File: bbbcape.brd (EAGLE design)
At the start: 54.6 x 71.8 mm, 25 parts

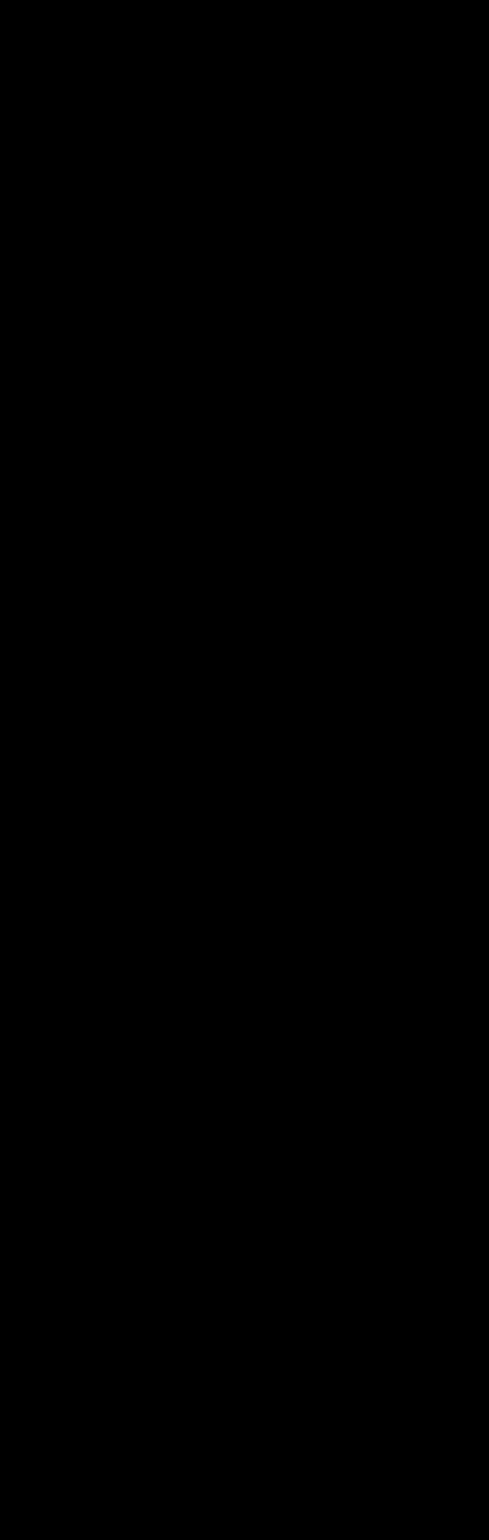
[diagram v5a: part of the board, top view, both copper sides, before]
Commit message: Added and connected firing circuit.
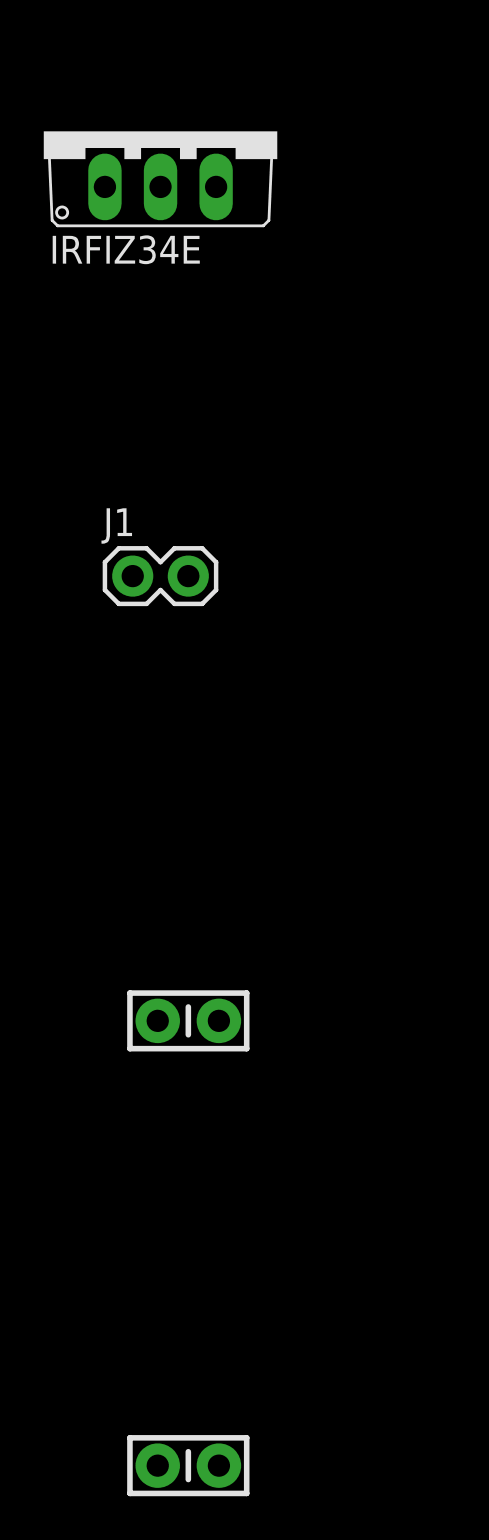
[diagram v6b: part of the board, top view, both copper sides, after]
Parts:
- added C2, C3: (no value), SparkFun-Capacitors:CAP-PTH-SMALL-KIT
- added IRFIZ34E: (no value), adafruit:TO220V
- added J1: (no value), SparkFun-Connectors:1X02
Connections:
- removed net 6V5: 6V5O.1, 6V5O.2
- removed net N$1: 5VI.1, 5VI.2, 6V5I.1, 6V5I.2, BATT.2, C1.1
- new net FEU: BBB.69, IRFIZ34E.1
- new net N$3: IRFIZ34E.2, J1.1
- new net VBAT: 5VI.1, 5VI.2, 6V5I.1, 6V5I.2, BATT.2, C1.1, C2.2
- net GND: now also C2.1, C3.2, IRFIZ34E.3
- net VCC: now also 6V5O.1, 6V5O.2, C3.1, J1.2
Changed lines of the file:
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@@
 <element name="R8" library="SparkFun-Passives" package="AXIAL-0.3" value="670" x="-78.74" y="-257.81"/>
 <element name="R9" library="SparkFun-Passives" package="AXIAL-0.3" value="1k" x="-78.74" y="-276.86"/>
+<element name="IRFIZ34E" library="adafruit" package="TO220V" value="" x="-81.28" y="-292.1"/>
+<element name="J1" library="SparkFun-Connectors" package="1X02" value="" x="-82.55" y="-312.42"/>
+<element name="C2" library="SparkFun-Capacitors" package="CAP-PTH-SMALL-KIT" value="" x="-80.01" y="-332.74">
+<attribute name="PROD_ID" value="CAP-08370" x="-80.01" y="-332.74" size="1.778" layer="27" display="off"/>
+</element>
+<element name="C3" library="SparkFun-Capacitors" package="CAP-PTH-SMALL-KIT" value="" x="-80.01" y="-353.06">
+<attribute name="PROD_ID" value="CAP-08370" x="-80.01" y="-353.06" size="1.778" layer="27" display="off"/>
+</element>
 </elements>
 <signals>
@@
 <contactref element="R9" pad="P$1"/>
 <contactref element="SHLD1" pad="8"/>
+<contactref element="C2" pad="1"/>
+<contactref element="IRFIZ34E" pad="3"/>
+<contactref element="C3" pad="2"/>
 <wire x1="-82.55" y1="-200.66" x2="-82.55" y2="-162.56" width="0" layer="19" extent="1-1"/>
 <wire x1="-82.55" y1="-238.76" x2="-82.55" y2="-200.66" width="0" layer="19" extent="1-1"/>
 <wire x1="-82.55" y1="-276.86" x2="-82.55" y2="-238.76" width="0" layer="19" extent="1-1"/>
+<wire x1="-78.74" y1="-294.64" x2="-82.55" y2="-276.86" width="0" layer="19" extent="1-1"/>
+<wire x1="-81.407" y1="-332.74" x2="-78.74" y2="-294.64" width="0" layer="19" extent="1-1"/>
+<wire x1="-78.613" y1="-353.06" x2="-81.407" y2="-332.74" width="0" layer="19" extent="1-1"/>
 <wire x1="-82.55" y1="-67.31" x2="-82.55" y2="-162.56" width="0" layer="19" extent="1-1"/>
 <wire x1="-82.55" y1="-48.26" x2="-82.55" y2="-67.31" width="0" layer="19" extent="1-1"/>
@@
 <wire x1="-77.47" y1="90.17" x2="-74.93" y2="90.17" width="0" layer="19" extent="1-1"/>
 </signal>
-<signal name="N$1">
+<signal name="VBAT">
 <contactref element="BATT" pad="2"/>
 <contactref element="5VI" pad="1"/>
@@
 <contactref element="6V5I" pad="1"/>
 <contactref element="C1" pad="1"/>
+<contactref element="C2" pad="2"/>
+<wire x1="-72.39" y1="3.81" x2="-78.613" y2="-332.74" width="0" layer="19" extent="1-1"/>
 <wire x1="-80.01" y1="90.17" x2="-72.39" y2="3.81" width="0" layer="19" extent="1-1"/>
 <wire x1="-82.55" y1="90.17" x2="-80.01" y2="90.17" width="0" layer="19" extent="1-1"/>
@@
 <wire x1="-49.53" y1="90.17" x2="-52.07" y2="95.25" width="0" layer="19" extent="1-1"/>
 <wire x1="-46.99" y1="90.17" x2="-49.53" y2="90.17" width="0" layer="19" extent="1-1"/>
-</signal>
-<signal name="6V5">
-<contactref element="6V5O" pad="1"/>
-<contactref element="6V5O" pad="2"/>
-<wire x1="-27.94" y1="95.25" x2="-25.4" y2="95.25" width="0" layer="19" extent="1-1"/>
 </signal>
 <signal name="5V">
@@
 <signal name="VCC">
 <contactref element="CAM" pad="2"/>
+<contactref element="6V5O" pad="1"/>
+<contactref element="6V5O" pad="2"/>
+<contactref element="C3" pad="1"/>
+<contactref element="J1" pad="2"/>
+<wire x1="-80.01" y1="-312.42" x2="-81.407" y2="-353.06" width="0" layer="19" extent="1-1"/>
+<wire x1="-80.01" y1="-48.26" x2="-80.01" y2="-312.42" width="0" layer="19" extent="1-1"/>
+<wire x1="-27.94" y1="95.25" x2="-80.01" y2="-48.26" width="0" layer="19" extent="1-1"/>
+<wire x1="-25.4" y1="95.25" x2="-27.94" y2="95.25" width="0" layer="19" extent="1-1"/>
 </signal>
 <signal name="UART1_TX">
@@
 <wire x1="-66.04" y1="90.17" x2="-63.5" y2="90.17" width="0" layer="19" extent="1-1"/>
 </signal>
+<signal name="N$3">
+<contactref element="IRFIZ34E" pad="2"/>
+<contactref element="J1" pad="1"/>
+<wire x1="-81.28" y1="-294.64" x2="-82.55" y2="-312.42" width="0" layer="19" extent="1-1"/>
+</signal>
+<signal name="FEU">
+<contactref element="BBB" pad="69"/>
+<contactref element="IRFIZ34E" pad="1"/>
+<wire x1="52.07" y1="29.21" x2="-83.82" y2="-294.64" width="0" layer="19" extent="1-1"/>
+</signal>
 </signals>

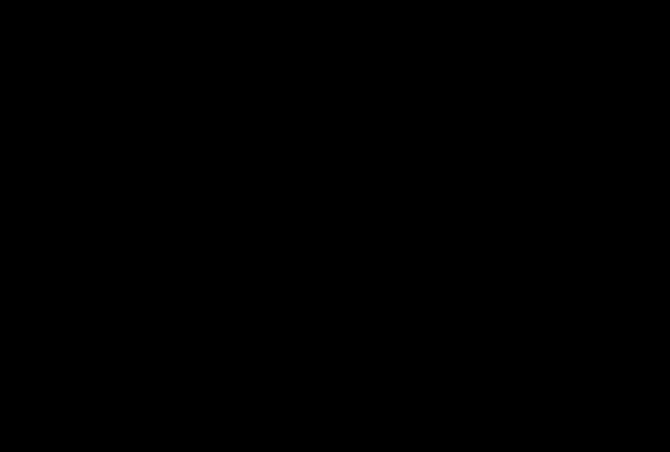
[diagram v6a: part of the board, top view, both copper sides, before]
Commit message: Added reset button (on BAR_GA, P8_10).
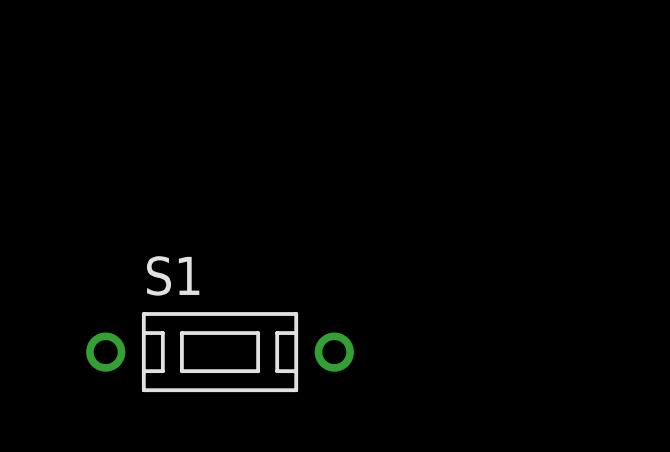
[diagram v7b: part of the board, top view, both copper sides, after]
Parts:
- added S1: TACTILE-SPST-6MM-SLIM, michel:6MM-SLIM
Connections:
- net BAR_GA: now also S1.P$2
- net BCOM: now also S1.P$1
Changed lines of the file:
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@@
 <attribute name="PROD_ID" value="CAP-08370" x="-80.01" y="-353.06" size="1.778" layer="27" display="off"/>
 </element>
+<element name="S1" library="michel" package="6MM-SLIM" value="TACTILE-SPST-6MM-SLIM" x="-81.28" y="-370.84"/>
 </elements>
 <signals>
@@
 <contactref element="R1" pad="P$1"/>
 <contactref element="BBB" pad="12"/>
+<contactref element="S1" pad="P$1"/>
+<wire x1="1.27" y1="13.97" x2="-85.09" y2="-370.84" width="0" layer="19" extent="1-1"/>
+<wire x1="-41.91" y1="95.25" x2="1.27" y2="13.97" width="0" layer="19" extent="1-1"/>
 <wire x1="-66.04" y1="95.25" x2="-41.91" y2="95.25" width="0" layer="19" extent="1-1"/>
-<wire x1="1.27" y1="13.97" x2="-41.91" y2="95.25" width="0" layer="19" extent="1-1"/>
 </signal>
 <signal name="BAV_DR">
@@
 <contactref element="BPR" pad="5"/>
 <contactref element="BBB" pad="10"/>
-<wire x1="1.27" y1="11.43" x2="-31.75" y2="95.25" width="0" layer="19" extent="1-1"/>
+<contactref element="S1" pad="P$2"/>
+<wire x1="1.27" y1="11.43" x2="-77.47" y2="-370.84" width="0" layer="19" extent="1-1"/>
+<wire x1="-31.75" y1="95.25" x2="1.27" y2="11.43" width="0" layer="19" extent="1-1"/>
 </signal>
 <signal name="3.3V">

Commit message: Added new DC-DC converter symbol (instead of headers).
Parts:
- removed 5VI, 5VO, 6V5I, 6V5O: (no value), SparkFun-Connectors:1X06
- added U5V, U6V5: SEEED-MP1584, michel:SEEED-MP1584
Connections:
- net GND: now also U5V.IN0+, U5V.IN1+, U5V.OUT0+, U5V.OUT1+, U6V5.IN0-, U6V5.IN1-, U6V5.OUT0-, U6V5.OUT1-; no longer 5VI.3, 5VI.4, 5VI.5, 5VI.6, 5VO.3, 5VO.4, 5VO.5, 5VO.6, 6V5I.3, 6V5I.4, 6V5I.5, 6V5I.6, 6V5O.3, 6V5O.4, 6V5O.5, 6V5O.6
- net VBAT: now also U5V.IN0-, U5V.IN1-, U6V5.IN0+, U6V5.IN1+; no longer 5VI.1, 5VI.2, 6V5I.1, 6V5I.2
- net VCC: now also U6V5.OUT0+, U6V5.OUT1+; no longer 6V5O.1, 6V5O.2
- net VDD: now also U5V.OUT0-, U5V.OUT1-; no longer 5VO.1, 5VO.2
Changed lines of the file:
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@@
 </autorouter>
 <elements>
-<element name="5VI" library="SparkFun-Connectors" package="1X06" value="" x="-49.53" y="90.17">
-<attribute name="PROD_ID" value="CONN-08437" x="-49.53" y="90.17" size="1.778" layer="27" display="off"/>
-</element>
-<element name="5VO" library="SparkFun-Connectors" package="1X06" value="" x="-66.04" y="90.17">
-<attribute name="PROD_ID" value="CONN-08437" x="-66.04" y="90.17" size="1.778" layer="27" display="off"/>
-</element>
-<element name="6V5I" library="SparkFun-Connectors" package="1X06" value="" x="-82.55" y="90.17">
-<attribute name="PROD_ID" value="CONN-08437" x="-82.55" y="90.17" size="1.778" layer="27" display="off"/>
-</element>
-<element name="6V5O" library="SparkFun-Connectors" package="1X06" value="" x="-27.94" y="95.25">
-<attribute name="PROD_ID" value="CONN-08437" x="-27.94" y="95.25" size="1.778" layer="27" display="off"/>
-</element>
 <element name="BATT" library="SparkFun-Connectors" package="1X02" value="" x="-54.61" y="95.25"/>
 <element name="BBB" library="adafruit" package="BEAGLEBONE_SHIELD" value="BEAGLEBONE_OUTLINE" x="-0.635" y="-17.78"/>
@@
 </element>
 <element name="S1" library="michel" package="6MM-SLIM" value="TACTILE-SPST-6MM-SLIM" x="-81.28" y="-370.84"/>
+<element name="U6V5" library="michel" package="SEEED-MP1584" value="SEEED-MP1584" x="-74.93" y="-391.16"/>
+<element name="U5V" library="michel" package="SEEED-MP1584" value="SEEED-MP1584" x="-74.93" y="-417.83"/>
 </elements>
 <signals>
@@
 <contactref element="BATT" pad="1"/>
 <contactref element="C1" pad="2"/>
-<contactref element="6V5I" pad="3"/>
-<contactref element="6V5I" pad="4"/>
-<contactref element="6V5I" pad="5"/>
-<contactref element="6V5I" pad="6"/>
-<contactref element="6V5O" pad="3"/>
-<contactref element="6V5O" pad="6"/>
-<contactref element="6V5O" pad="5"/>
-<contactref element="6V5O" pad="4"/>
-<contactref element="5VI" pad="3"/>
-<contactref element="5VI" pad="4"/>
-<contactref element="5VI" pad="5"/>
-<contactref element="5VI" pad="6"/>
-<contactref element="5VO" pad="3"/>
-<contactref element="5VO" pad="4"/>
-<contactref element="5VO" pad="5"/>
-<contactref element="5VO" pad="6"/>
 <contactref element="CAM" pad="1"/>
 <contactref element="R3" pad="P$1"/>
@@
 <contactref element="IRFIZ34E" pad="3"/>
 <contactref element="C3" pad="2"/>
-<wire x1="-82.55" y1="-200.66" x2="-82.55" y2="-162.56" width="0" layer="19" extent="1-1"/>
-<wire x1="-82.55" y1="-238.76" x2="-82.55" y2="-200.66" width="0" layer="19" extent="1-1"/>
-<wire x1="-82.55" y1="-276.86" x2="-82.55" y2="-238.76" width="0" layer="19" extent="1-1"/>
-<wire x1="-78.74" y1="-294.64" x2="-82.55" y2="-276.86" width="0" layer="19" extent="1-1"/>
-<wire x1="-81.407" y1="-332.74" x2="-78.74" y2="-294.64" width="0" layer="19" extent="1-1"/>
-<wire x1="-78.613" y1="-353.06" x2="-81.407" y2="-332.74" width="0" layer="19" extent="1-1"/>
+<contactref element="U6V5" pad="OUT0-"/>
+<contactref element="U6V5" pad="OUT1-"/>
+<contactref element="U6V5" pad="IN0-"/>
+<contactref element="U6V5" pad="IN1-"/>
+<contactref element="U5V" pad="OUT1+"/>
+<contactref element="U5V" pad="OUT0+"/>
+<contactref element="U5V" pad="IN1+"/>
+<contactref element="U5V" pad="IN0+"/>
+<wire x1="-84.18" y1="-424.455" x2="-84.18" y2="-421.83" width="0" layer="19" extent="1-1"/>
+<wire x1="-65.68" y1="-424.455" x2="-84.18" y2="-424.455" width="0" layer="19" extent="1-1"/>
+<wire x1="-65.68" y1="-421.83" x2="-65.68" y2="-424.455" width="0" layer="19" extent="1-1"/>
+<wire x1="-84.18" y1="-387.16" x2="-84.18" y2="-421.83" width="0" layer="19" extent="1-1"/>
+<wire x1="-84.18" y1="-384.535" x2="-84.18" y2="-387.16" width="0" layer="19" extent="1-1"/>
+<wire x1="-65.68" y1="-387.16" x2="-84.18" y2="-387.16" width="0" layer="19" extent="1-1"/>
+<wire x1="-65.68" y1="-384.535" x2="-65.68" y2="-387.16" width="0" layer="19" extent="1-1"/>
+<wire x1="-78.613" y1="-353.06" x2="-84.18" y2="-384.535" width="0" layer="19" extent="1-1"/>
+<wire x1="-81.407" y1="-332.74" x2="-78.613" y2="-353.06" width="0" layer="19" extent="1-1"/>
+<wire x1="-78.74" y1="-294.64" x2="-81.407" y2="-332.74" width="0" layer="19" extent="1-1"/>
+<wire x1="-82.55" y1="-276.86" x2="-78.74" y2="-294.64" width="0" layer="19" extent="1-1"/>
+<wire x1="-82.55" y1="-238.76" x2="-82.55" y2="-276.86" width="0" layer="19" extent="1-1"/>
+<wire x1="-82.55" y1="-200.66" x2="-82.55" y2="-238.76" width="0" layer="19" extent="1-1"/>
+<wire x1="-82.55" y1="-162.56" x2="-82.55" y2="-200.66" width="0" layer="19" extent="1-1"/>
 <wire x1="-82.55" y1="-67.31" x2="-82.55" y2="-162.56" width="0" layer="19" extent="1-1"/>
 <wire x1="-82.55" y1="-48.26" x2="-82.55" y2="-67.31" width="0" layer="19" extent="1-1"/>
@@
 <wire x1="49.53" y1="54.61" x2="52.07" y2="54.61" width="0" layer="19" extent="1-1"/>
 <wire x1="-15.24" y1="90.17" x2="49.53" y2="57.15" width="0" layer="19" extent="1-1"/>
-<wire x1="-15.24" y1="95.25" x2="-15.24" y2="90.17" width="0" layer="19" extent="1-1"/>
-<wire x1="-17.78" y1="95.25" x2="-15.24" y2="95.25" width="0" layer="19" extent="1-1"/>
-<wire x1="-20.32" y1="95.25" x2="-17.78" y2="95.25" width="0" layer="19" extent="1-1"/>
-<wire x1="-22.86" y1="95.25" x2="-20.32" y2="95.25" width="0" layer="19" extent="1-1"/>
-<wire x1="-36.83" y1="90.17" x2="-22.86" y2="95.25" width="0" layer="19" extent="1-1"/>
-<wire x1="-39.37" y1="90.17" x2="-36.83" y2="90.17" width="0" layer="19" extent="1-1"/>
-<wire x1="-41.91" y1="90.17" x2="-39.37" y2="90.17" width="0" layer="19" extent="1-1"/>
-<wire x1="-44.45" y1="90.17" x2="-41.91" y2="90.17" width="0" layer="19" extent="1-1"/>
-<wire x1="-48.26" y1="95.25" x2="-44.45" y2="90.17" width="0" layer="19" extent="1-1"/>
+<wire x1="-48.26" y1="95.25" x2="-15.24" y2="90.17" width="0" layer="19" extent="1-1"/>
 <wire x1="-54.61" y1="95.25" x2="-48.26" y2="95.25" width="0" layer="19" extent="1-1"/>
-<wire x1="-53.34" y1="90.17" x2="-54.61" y2="95.25" width="0" layer="19" extent="1-1"/>
-<wire x1="-55.88" y1="90.17" x2="-53.34" y2="90.17" width="0" layer="19" extent="1-1"/>
-<wire x1="-58.42" y1="90.17" x2="-55.88" y2="90.17" width="0" layer="19" extent="1-1"/>
-<wire x1="-60.96" y1="90.17" x2="-58.42" y2="90.17" width="0" layer="19" extent="1-1"/>
-<wire x1="-69.85" y1="90.17" x2="-60.96" y2="90.17" width="0" layer="19" extent="1-1"/>
-<wire x1="-72.39" y1="90.17" x2="-69.85" y2="90.17" width="0" layer="19" extent="1-1"/>
-<wire x1="-74.93" y1="90.17" x2="-72.39" y2="90.17" width="0" layer="19" extent="1-1"/>
-<wire x1="-77.47" y1="90.17" x2="-74.93" y2="90.17" width="0" layer="19" extent="1-1"/>
 </signal>
 <signal name="VBAT">
 <contactref element="BATT" pad="2"/>
-<contactref element="5VI" pad="1"/>
-<contactref element="5VI" pad="2"/>
-<contactref element="6V5I" pad="2"/>
-<contactref element="6V5I" pad="1"/>
+<contactref element="C2" pad="2"/>
+<contactref element="U5V" pad="IN1-"/>
+<contactref element="U5V" pad="IN0-"/>
+<contactref element="U6V5" pad="IN0+"/>
+<contactref element="U6V5" pad="IN1+"/>
 <contactref element="C1" pad="1"/>
-<contactref element="C2" pad="2"/>
+<wire x1="-84.18" y1="-411.205" x2="-84.18" y2="-413.83" width="0" layer="19" extent="1-1"/>
+<wire x1="-84.18" y1="-397.785" x2="-84.18" y2="-411.205" width="0" layer="19" extent="1-1"/>
+<wire x1="-84.18" y1="-395.16" x2="-84.18" y2="-397.785" width="0" layer="19" extent="1-1"/>
+<wire x1="-78.613" y1="-332.74" x2="-84.18" y2="-395.16" width="0" layer="19" extent="1-1"/>
 <wire x1="-72.39" y1="3.81" x2="-78.613" y2="-332.74" width="0" layer="19" extent="1-1"/>
-<wire x1="-80.01" y1="90.17" x2="-72.39" y2="3.81" width="0" layer="19" extent="1-1"/>
-<wire x1="-82.55" y1="90.17" x2="-80.01" y2="90.17" width="0" layer="19" extent="1-1"/>
-<wire x1="-52.07" y1="95.25" x2="-80.01" y2="90.17" width="0" layer="19" extent="1-1"/>
-<wire x1="-49.53" y1="90.17" x2="-52.07" y2="95.25" width="0" layer="19" extent="1-1"/>
-<wire x1="-46.99" y1="90.17" x2="-49.53" y2="90.17" width="0" layer="19" extent="1-1"/>
+<wire x1="-52.07" y1="95.25" x2="-72.39" y2="3.81" width="0" layer="19" extent="1-1"/>
 </signal>
 <signal name="5V">
@@
 <signal name="VCC">
 <contactref element="CAM" pad="2"/>
-<contactref element="6V5O" pad="1"/>
-<contactref element="6V5O" pad="2"/>
 <contactref element="C3" pad="1"/>
 <contactref element="J1" pad="2"/>
+<contactref element="U6V5" pad="OUT0+"/>
+<contactref element="U6V5" pad="OUT1+"/>
+<wire x1="-65.68" y1="-395.16" x2="-65.68" y2="-397.785" width="0" layer="19" extent="1-1"/>
+<wire x1="-81.407" y1="-353.06" x2="-65.68" y2="-395.16" width="0" layer="19" extent="1-1"/>
 <wire x1="-80.01" y1="-312.42" x2="-81.407" y2="-353.06" width="0" layer="19" extent="1-1"/>
 <wire x1="-80.01" y1="-48.26" x2="-80.01" y2="-312.42" width="0" layer="19" extent="1-1"/>
-<wire x1="-27.94" y1="95.25" x2="-80.01" y2="-48.26" width="0" layer="19" extent="1-1"/>
-<wire x1="-25.4" y1="95.25" x2="-27.94" y2="95.25" width="0" layer="19" extent="1-1"/>
 </signal>
 <signal name="UART1_TX">
@@
 <signal name="VDD">
 <contactref element="BBB" pad="51"/>
-<contactref element="5VO" pad="1"/>
-<contactref element="5VO" pad="2"/>
 <contactref element="BBB" pad="52"/>
-<wire x1="49.53" y1="6.35" x2="52.07" y2="6.35" width="0" layer="19" extent="1-1"/>
-<wire x1="-63.5" y1="90.17" x2="49.53" y2="6.35" width="0" layer="19" extent="1-1"/>
-<wire x1="-66.04" y1="90.17" x2="-63.5" y2="90.17" width="0" layer="19" extent="1-1"/>
+<contactref element="U5V" pad="OUT1-"/>
+<contactref element="U5V" pad="OUT0-"/>
+<wire x1="-65.68" y1="-411.205" x2="-65.68" y2="-413.83" width="0" layer="19" extent="1-1"/>
+<wire x1="49.53" y1="6.35" x2="-65.68" y2="-411.205" width="0" layer="19" extent="1-1"/>
+<wire x1="52.07" y1="6.35" x2="49.53" y2="6.35" width="0" layer="19" extent="1-1"/>
 </signal>
 <signal name="N$3">
